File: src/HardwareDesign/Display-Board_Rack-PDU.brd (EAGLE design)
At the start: 81.3 x 35.6 mm, 46 parts

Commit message: first order send to JLCPCB
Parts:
- BUT+1, BUT-1, BUT_PWR1, BUT_SET1: value ADTSMW64 -> TC-6601-5.0-160
- ETH: value (none) -> XL-2012UBC
- FAULT: value (none) -> XL-2012SURC
- IC1: value (none) -> MCP23S18-E/MJ
- R26, R27: value 742C083103JP -> 4D03WGJ0102T5E 1K
- R28, R29, R30: value 10K -> 1K
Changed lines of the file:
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@@
 <drawing>
 <settings>
-<setting alwaysvectorfont="yes"/>
+<setting alwaysvectorfont="no"/>
 <setting verticaltext="up"/>
 </settings>
@@
 <element name="CON3" library="ds_con" package="2X7-SIDE" package3d_urn="urn:adsk.eagle:package:46762478/3" value="" x="50.8" y="0" smashed="yes" rot="R270"/>
 <element name="CON4" library="ds_con" package="2X7-SIDE" package3d_urn="urn:adsk.eagle:package:46762478/3" value="" x="71.12" y="0" smashed="yes" rot="R270"/>
-<element name="BUT+1" library="Wurth_Switch_WS-TASV" library_urn="urn:adsk.eagle:library:18304196" package="430182043816" package3d_urn="urn:adsk.eagle:package:18304300/2" value="ADTSMW64" x="43.18" y="27.34" smashed="yes" rot="MR0">
+<element name="BUT+1" library="Wurth_Switch_WS-TASV" library_urn="urn:adsk.eagle:library:18304196" package="430182043816" package3d_urn="urn:adsk.eagle:package:18304300/2" value="TC-6601-5.0-160" x="43.18" y="27.34" smashed="yes" rot="MR0">
 <attribute name="DATASHEET-URL" value="https://www.we-online.com/redexpert/spec/430182043816?ae" x="43.18" y="27.34" size="1.778" layer="28" rot="MR0" display="off"/>
 <attribute name="HEIGHT" value="4.3mm" x="43.18" y="27.34" size="1.778" layer="28" rot="MR0" display="off"/>
@@
 <attribute name="VALUE" x="40.459" y="26.999" size="1.016" layer="27" rot="R270"/>
 </element>
-<element name="BUT-1" library="Wurth_Switch_WS-TASV" library_urn="urn:adsk.eagle:library:18304196" package="430182043816" package3d_urn="urn:adsk.eagle:package:18304300/2" value="ADTSMW64" x="43.18" y="17.78" smashed="yes" rot="MR180">
+<element name="BUT-1" library="Wurth_Switch_WS-TASV" library_urn="urn:adsk.eagle:library:18304196" package="430182043816" package3d_urn="urn:adsk.eagle:package:18304300/2" value="TC-6601-5.0-160" x="43.18" y="17.78" smashed="yes" rot="MR180">
 <attribute name="DATASHEET-URL" value="https://www.we-online.com/redexpert/spec/430182043816?ae" x="33.02" y="5.08" size="1.778" layer="28" rot="MR180" display="off"/>
 <attribute name="HEIGHT" value="4.3mm" x="33.02" y="5.08" size="1.778" layer="28" rot="MR180" display="off"/>
@@
 <attribute name="VALUE" x="44.069" y="15.621" size="1.016" layer="27" rot="R90"/>
 </element>
-<element name="BUT_SET1" library="Wurth_Switch_WS-TASV" library_urn="urn:adsk.eagle:library:18304196" package="430182043816" package3d_urn="urn:adsk.eagle:package:18304300/2" value="ADTSMW64" x="30.48" y="22.86" smashed="yes" rot="MR180">
+<element name="BUT_SET1" library="Wurth_Switch_WS-TASV" library_urn="urn:adsk.eagle:library:18304196" package="430182043816" package3d_urn="urn:adsk.eagle:package:18304300/2" value="TC-6601-5.0-160" x="30.48" y="22.86" smashed="yes" rot="MR180">
 <attribute name="DATASHEET-URL" value="https://www.we-online.com/redexpert/spec/430182043816?ae" x="19.05" y="10.16" size="1.778" layer="28" rot="MR180" display="off"/>
 <attribute name="HEIGHT" value="4.3mm" x="19.05" y="10.16" size="1.778" layer="28" rot="MR180" display="off"/>
@@
 <attribute name="VALUE" x="34.671" y="18.161" size="1.016" layer="27" rot="R90"/>
 </element>
-<element name="BUT_PWR1" library="Wurth_Switch_WS-TASV" library_urn="urn:adsk.eagle:library:18304196" package="430182043816" package3d_urn="urn:adsk.eagle:package:18304300/2" value="ADTSMW64" x="8.89" y="7.62" smashed="yes" rot="MR0">
+<element name="BUT_PWR1" library="Wurth_Switch_WS-TASV" library_urn="urn:adsk.eagle:library:18304196" package="430182043816" package3d_urn="urn:adsk.eagle:package:18304300/2" value="TC-6601-5.0-160" x="8.89" y="7.62" smashed="yes" rot="MR0">
 <attribute name="DATASHEET-URL" value="https://www.we-online.com/redexpert/spec/430182043816?ae" x="30.48" y="21.59" size="1.778" layer="28" rot="MR0" display="off"/>
 <attribute name="HEIGHT" value="4.3mm" x="30.48" y="21.59" size="1.778" layer="28" rot="MR0" display="off"/>
@@
 <attribute name="VALUE" x="12.092075" y="27.94" size="1.016" layer="27" rot="R135"/>
 </element>
-<element name="IC1" library="ds_ic_peripherals" package="QFN50P400X400X100-25T265" package3d_urn="urn:adsk.eagle:package:46683902/2" value="" x="14.04439375" y="30.449184375" smashed="yes" rot="R315">
+<element name="IC1" library="ds_ic_peripherals" package="QFN50P400X400X100-25T265" package3d_urn="urn:adsk.eagle:package:46683902/2" value="MCP23S18-E/MJ" x="14.04439375" y="30.449184375" smashed="yes" rot="R315">
 <attribute name="NAME" x="17.55988125" y="28.483228125" size="1.27" layer="25" rot="R45" align="bottom-center"/>
 <attribute name="VALUE" x="6.541353125" y="33.72245" size="1.27" layer="27" rot="R315" align="top-center"/>
@@
 <attribute name="VALUE" x="58.03" y="12.98" size="0.8128" layer="28" rot="MR180"/>
 </element>
-<element name="R26" library="Resistor Array" library_urn="urn:adsk.eagle:library:16491332" package="742C083103JP" package3d_urn="urn:adsk.eagle:package:16445849/4" value="742C083103JP" x="21.844" y="28.448" smashed="yes" rot="R270">
+<element name="R26" library="Resistor Array" library_urn="urn:adsk.eagle:library:16491332" package="742C083103JP" package3d_urn="urn:adsk.eagle:package:16445849/4" value="4D03WGJ0102T5E 1K" x="21.844" y="28.448" smashed="yes" rot="R270">
 <attribute name="CREATED_BY" value="PCBLayout.com" x="21.844" y="28.448" size="1.778" layer="27" rot="R270" display="off"/>
 <attribute name="DIGIKEY_PN" value="742C083103JPTR-ND" x="21.844" y="28.448" size="1.778" layer="27" rot="R270" display="off"/>
@@
 <attribute name="VALUE" x="19.454390625" y="30.222390625" size="0.66234375" layer="27" rot="R270"/>
 </element>
-<element name="R27" library="Resistor Array" library_urn="urn:adsk.eagle:library:16491332" package="742C083103JP" package3d_urn="urn:adsk.eagle:package:16445849/4" value="742C083103JP" x="21.844" y="32.512" smashed="yes" rot="R270">
+<element name="R27" library="Resistor Array" library_urn="urn:adsk.eagle:library:16491332" package="742C083103JP" package3d_urn="urn:adsk.eagle:package:16445849/4" value="4D03WGJ0102T5E 1K" x="21.844" y="32.512" smashed="yes" rot="R270">
 <attribute name="CREATED_BY" value="PCBLayout.com" x="21.844" y="32.512" size="1.778" layer="27" rot="R270" display="off"/>
 <attribute name="DIGIKEY_PN" value="742C083103JPTR-ND" x="21.844" y="32.512" size="1.778" layer="27" rot="R270" display="off"/>
@@
 <attribute name="VALUE" x="19.454390625" y="34.286390625" size="0.66234375" layer="27" rot="R270"/>
 </element>
-<element name="R28" library="ds_passive" package="0402" package3d_urn="urn:adsk.eagle:package:46683744/2" value="10K" x="4.26" y="22.8" smashed="yes" rot="R270">
+<element name="R28" library="ds_passive" package="0402" package3d_urn="urn:adsk.eagle:package:46683744/2" value="1K" x="4.26" y="22.8" smashed="yes" rot="R270">
 <attribute name="NAME" x="4.895" y="23.435" size="1.016" layer="25" rot="R270"/>
 <attribute name="VALUE" x="2.355" y="23.435" size="1.016" layer="27" rot="R270"/>
 </element>
-<element name="R29" library="ds_passive" package="0402" package3d_urn="urn:adsk.eagle:package:46683744/2" value="10K" x="9.98" y="33.55" smashed="yes" rot="R180">
+<element name="R29" library="ds_passive" package="0402" package3d_urn="urn:adsk.eagle:package:46683744/2" value="1K" x="9.98" y="33.55" smashed="yes" rot="R180">
 <attribute name="NAME" x="10.615" y="32.915" size="1.016" layer="25" rot="R180"/>
 <attribute name="VALUE" x="10.615" y="35.455" size="1.016" layer="27" rot="R180"/>
 </element>
-<element name="R30" library="ds_passive" package="0402" package3d_urn="urn:adsk.eagle:package:46683744/2" value="10K" x="4.24" y="16.26" smashed="yes" rot="R270">
+<element name="R30" library="ds_passive" package="0402" package3d_urn="urn:adsk.eagle:package:46683744/2" value="1K" x="4.24" y="16.26" smashed="yes" rot="R270">
 <attribute name="NAME" x="4.875" y="16.895" size="1.016" layer="25" rot="R270"/>
 <attribute name="VALUE" x="2.335" y="16.895" size="1.016" layer="27" rot="R270"/>
 </element>
-<element name="FAULT" library="led" library_urn="urn:adsk.eagle:library:259" package="CHIP-LED0805" package3d_urn="urn:adsk.eagle:package:15818/2" value="" x="18.04" y="33.54" smashed="yes" rot="MR90">
+<element name="FAULT" library="led" library_urn="urn:adsk.eagle:library:259" package="CHIP-LED0805" package3d_urn="urn:adsk.eagle:package:15818/2" value="XL-2012SURC" x="18.04" y="33.54" smashed="yes" rot="MR90">
 <attribute name="NAME" x="20.83" y="31.17" size="1.27" layer="26" rot="MR0"/>
 <attribute name="VALUE" x="16.77" y="36.08" size="1.27" layer="28" rot="MR180"/>
 </element>
-<element name="ETH" library="led" library_urn="urn:adsk.eagle:library:259" package="CHIP-LED0805" package3d_urn="urn:adsk.eagle:package:15818/2" value="" x="8.52" y="21.49" smashed="yes" rot="MR90">
+<element name="ETH" library="led" library_urn="urn:adsk.eagle:library:259" package="CHIP-LED0805" package3d_urn="urn:adsk.eagle:package:15818/2" value="XL-2012UBC" x="8.52" y="21.49" smashed="yes" rot="MR90">
 <attribute name="NAME" x="10.65" y="22.22" size="1.27" layer="26" rot="MR180"/>
 <attribute name="VALUE" x="7.25" y="24.03" size="1.27" layer="28" rot="MR180"/>

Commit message: generate Gerber files
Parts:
- moved C20 0.85 mm to (9.60, 8.29)
- moved R24 0.85 mm to (7.87, 8.29)
- moved C21 0.39 mm to (10.2, 28.7)
- moved C22 0.39 mm to (9.33, 27.8)
- moved R22 0.10 mm to (44.3, 16.3)
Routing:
- net SPI_MOSI: track 106.6 -> 107.8 mm
- net KEY_3: track 64.6 -> 65.9 mm
- net +3V3: track 234.7 -> 235.9 mm
- net KEY_0: track 39.6 -> 40.8 mm
- net KEY_1: track 29.1 -> 28.2 mm
- net SPI_SCK: track 103.7 -> 104.6 mm
- net GND: track 363.5 -> 362.6 mm

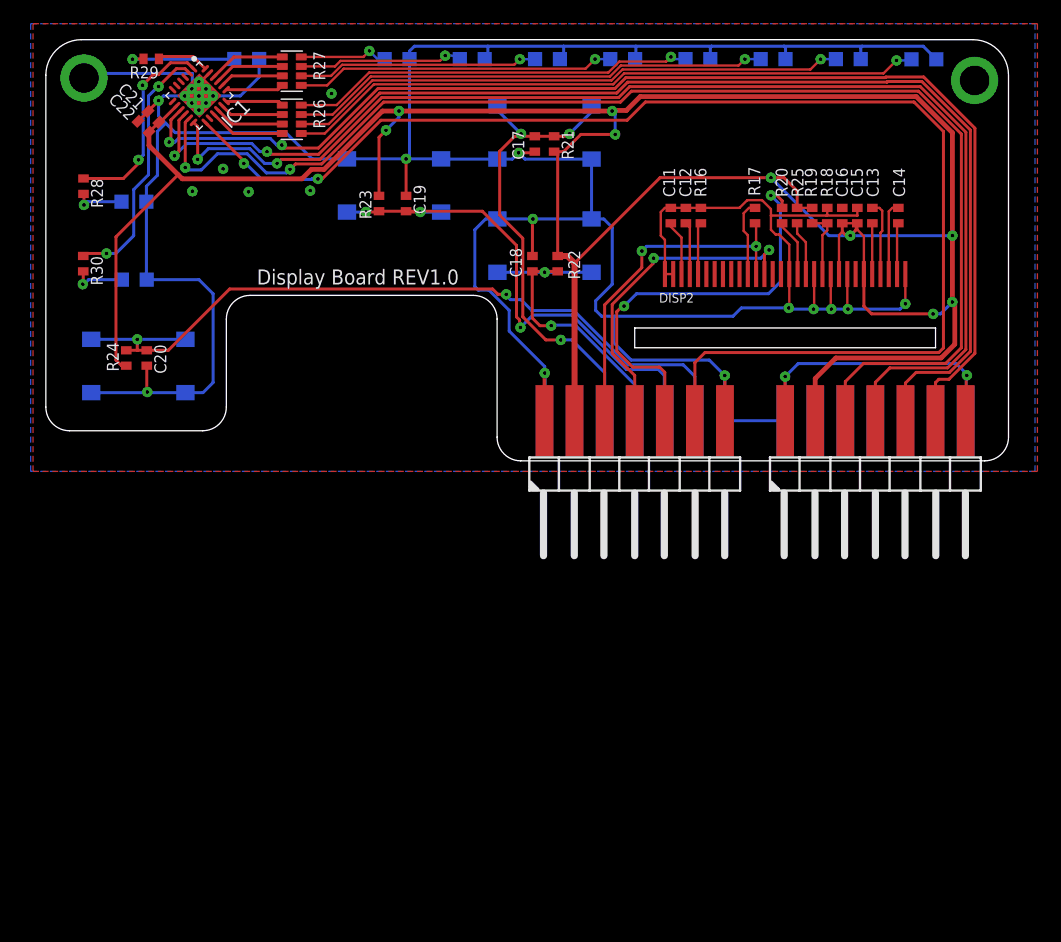
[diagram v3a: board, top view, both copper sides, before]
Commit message: start Displayboard rev 2
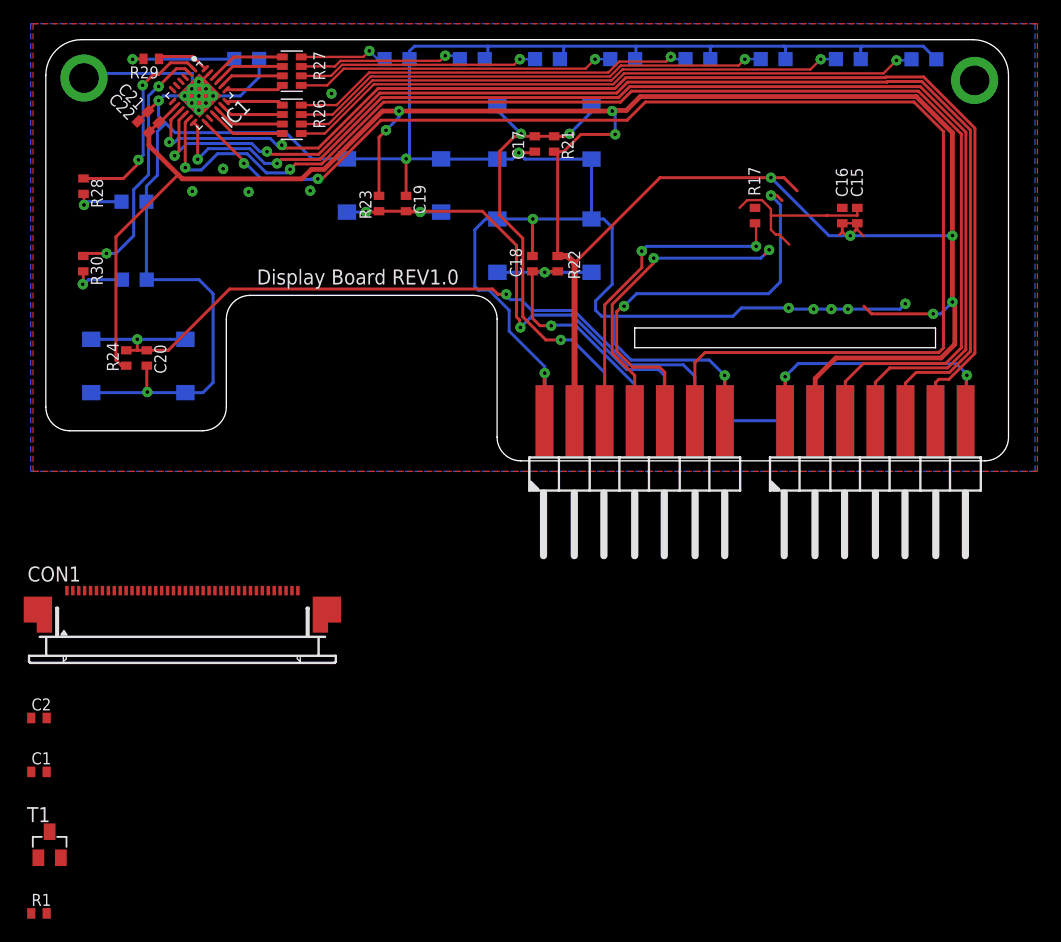
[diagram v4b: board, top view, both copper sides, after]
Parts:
- removed C11, C12: 100nF, ds_passive:0402
- removed C13, C14: 2.2uF, ds_passive:0402
- removed DISP2: 128X64OLED, ds_displays:UG2864
- removed R16: 390K, ds_passive:0402
- removed R18: DNI, ds_passive:0402
- removed R19, R20: 0R, ds_passive:0402
- removed R25: 10K, ds_passive:0402
- added C1: 10uF, ds_passive:C0402
- added C2: 100nF, ds_passive:C0402
- added CON1: 3.5IN_TFTLCD, ds_displays:FPC40
- added R1: 10K, ds_passive:0402
- added T1: BSS138, transistor-fet:SOT23
- C15: value 2.2uF -> 10uF; device ds_passive:0402 -> ds_passive:C0402
- C16: value 2.2uF -> 100nF; device ds_passive:0402 -> ds_passive:C0402
- C17, C18, C19, C20, C21, C22: device ds_passive:0402 -> ds_passive:C0402
- R17: value 0R -> 10K
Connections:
- removed net BS1: DISP2.11, R18.1, R19.2
- removed net N$22: C13.2, DISP2.5
- removed net N$35: C13.1, DISP2.4
- removed net N$36: C14.2, DISP2.3
- removed net N$37: C14.1, DISP2.2
- removed net N$38: DISP2.26, R16.1
- removed net N$39: C11.1, DISP2.28
- removed net N$40: C12.1, DISP2.27
- removed net N$41: DISP2.20, R17.1
- removed net N$49: DISP2.13, R25.2
- removed net RST: DISP2.14, R20.1
- new net CS: CON1.9
- new net MISO: CON1.14
- new net MOSI: CON1.13
- new net N$1: CON1.10, R17.2
- new net N$2: CON1.35
- new net N$3: CON1.36
- new net N$5: CON1.34, R1.2
- new net RES: CON1.15
- new net SCLK: CON1.11
- net +3V3: now also C1.1, C2.1, CON1.12, CON1.33, CON1.38, CON1.39, CON1.40, CON1.6, CON1.7; no longer DISP2.6, DISP2.9, R19.1, R25.1
- net DSP_RES: no longer R20.2
- net GND: now also C1.2, C2.2, CON1.16, CON1.17, CON1.18, CON1.19, CON1.20, CON1.21, CON1.22, CON1.23, CON1.24, CON1.25, CON1.26, CON1.27, CON1.28, CON1.29, CON1.30, CON1.31, CON1.32, CON1.37, CON1.5, R17.1; no longer C11.2, C12.2, DISP2.1, DISP2.10, DISP2.12, DISP2.15, DISP2.29, DISP2.30, DISP2.8, R16.2, R18.2
- net I2C_SCL: no longer DISP2.18
- net I2C_SDA: no longer DISP2.19, R17.2
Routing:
- net GND: track 362.6 -> 332.6 mm
- net +3V3: track 235.9 -> 224.0 mm
- net N$41: track 6.43 -> 0.00 mm
- net N$35: track 6.34 -> 0.00 mm
- net N$36: track 6.22 -> 0.00 mm
- net BS1: track 5.73 -> 0.00 mm
- net RST: track 4.83 -> 0.00 mm
- net N$39: track 4.66 -> 0.00 mm
- net N$49: track 4.59 -> 0.00 mm
- net N$40: track 4.43 -> 0.00 mm
- net N$38: track 4.39 -> 0.00 mm
- net N$37: track 4.34 -> 0.00 mm
- net N$22: track 4.30 -> 0.00 mm
- net I2C_SDA: track 29.8 -> 27.3 mm
- net I2C_SCL: track 28.2 -> 26.6 mm
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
